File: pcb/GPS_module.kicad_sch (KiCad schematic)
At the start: 1 part, among them U9 SAM-M10Q-00B

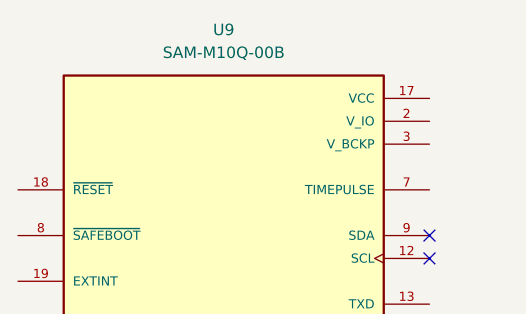
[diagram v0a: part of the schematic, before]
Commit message: Updated parts
Updated parts, most should be included at this point. Layout is not complete.
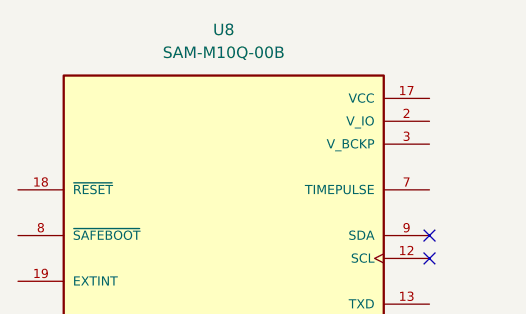
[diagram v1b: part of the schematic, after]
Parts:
- U8: renamed from U9; footprint SAM-M10Q-00B:XCVR_SAM-M10Q-00B -> SAM M10Q:XCVR_SAM-M10Q-00B
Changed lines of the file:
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@@
 		(on_board yes)
 		(dnp no)
-		(property "Reference" "#PWR089"
+		(property "Reference" "#PWR092"
 			(at 170.18 129.54 0)
 			(effects
@@
 			(project ""
 				(path "/ba7b4294-8d75-4b9e-892f-fb52727887ec/fc9e3a2d-4610-4d80-a238-b7d530352ab2"
-					(reference "#PWR089")
+					(reference "#PWR092")
 					(unit 1)
 				)
@@
 		(dnp no)
 		(fields_autoplaced yes)
-		(property "Reference" "U9"
+		(property "Reference" "U8"
 			(at 140.97 62.23 0)
 			(effects
@@
 			)
 		)
-		(property "Footprint" "SAM-M10Q-00B:XCVR_SAM-M10Q-00B"
+		(property "Footprint" "SAM M10Q:XCVR_SAM-M10Q-00B"
 			(at 140.97 85.09 0)
 			(effects
@@
 			(project "control-module"
 				(path "/ba7b4294-8d75-4b9e-892f-fb52727887ec/fc9e3a2d-4610-4d80-a238-b7d530352ab2"
-					(reference "U9")
+					(reference "U8")
 					(unit 1)
 				)

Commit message: Pre-fab update
Pre fab update
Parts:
- added C28: 100nF, Capacitor_SMD:C_0603_1608Metric_Pad1.08x0.95mm_HandSolder, symbol Device:C
- added C29: 1uF, Capacitor_SMD:C_0603_1608Metric_Pad1.08x0.95mm_HandSolder, symbol Device:C
- added C32: 4.7uF, Capacitor_SMD:C_0603_1608Metric, symbol Device:C
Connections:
- net GPS_TX: now reaches U8.13 (TXD)
- net GPS_RX: now reaches U8.14 (RXD)
- net +3.3V_radio: now reaches U8.17 (VCC)
- net +3.3V_radio: now also U8.18 (~{RESET}), U8.2 (V_IO), U8.3 (V_BCKP), C28.1, C29.1, C32.1
- net TIMEPULSE_OUT: now reaches U8.7 (TIMEPULSE)
- net GND renamed GNDD
- net GNDD: now also C28.2, C29.2, C32.2
- no-connect marks 2 -> 4
